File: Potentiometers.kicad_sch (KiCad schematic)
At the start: 20 parts, among them J10 AccelConn, J11 BrakeConn, J12 AccelConn2, J13 BrakeConn2

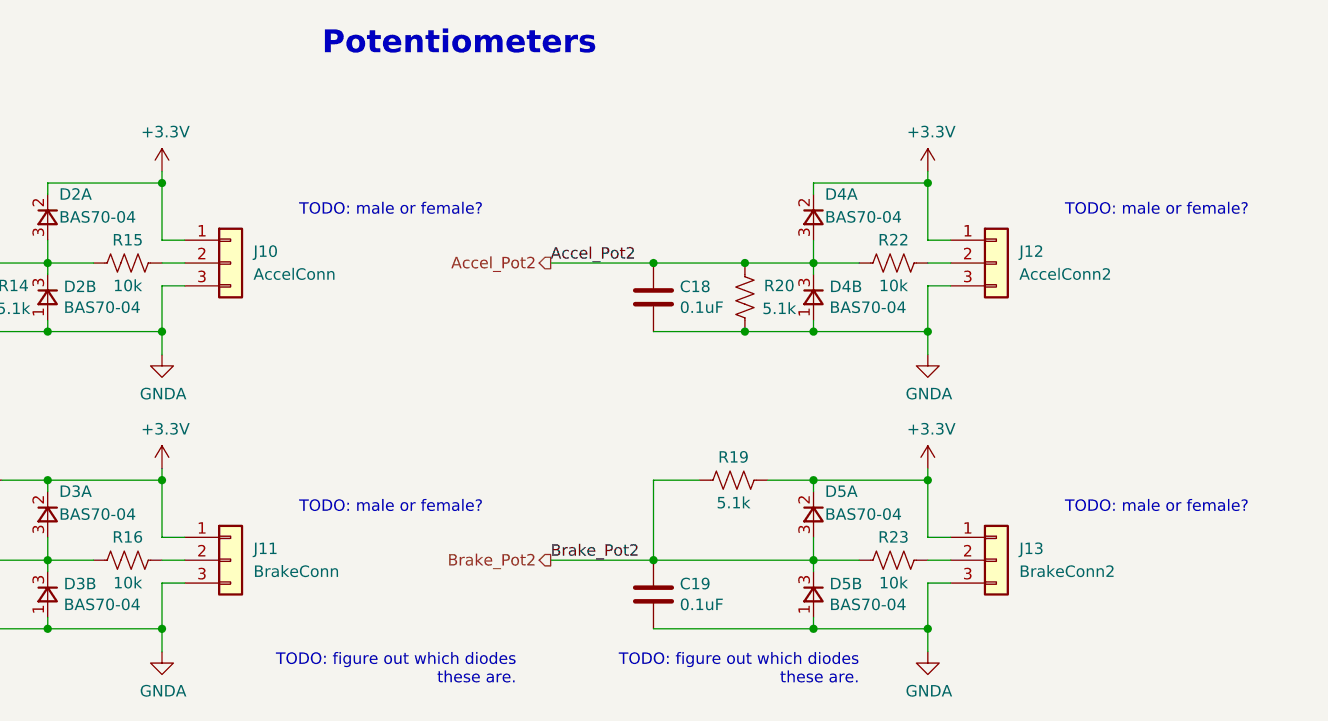
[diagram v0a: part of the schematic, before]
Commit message: Remove 12V isolator, swap CAN connector pins, etc.
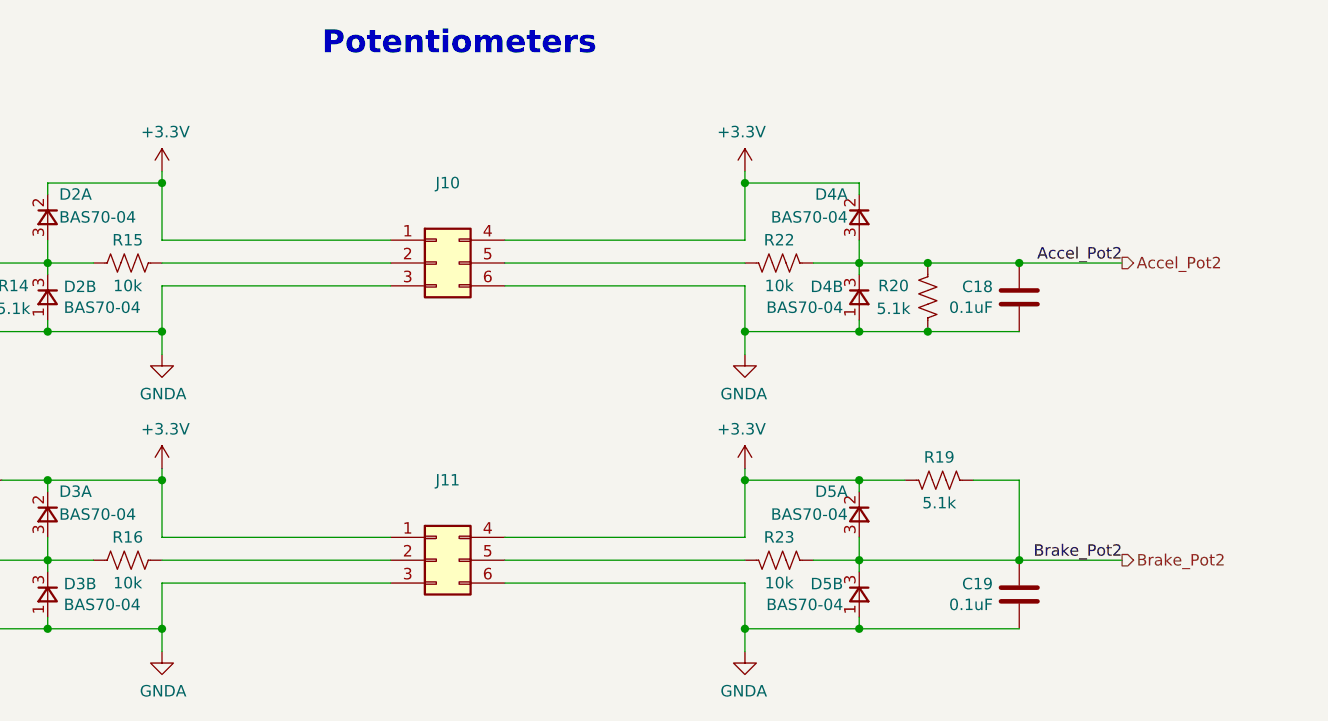
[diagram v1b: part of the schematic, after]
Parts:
- removed J10: AccelConn, UTSVT_Connectors:Molex_MicroFit3.0_1x3xP3.00mm_PolarizingPeg_Vertical, symbol Connector_Generic:Conn_01x03
- removed J11: BrakeConn, UTSVT_Connectors:Molex_MicroFit3.0_1x3xP3.00mm_PolarizingPeg_Vertical, symbol Connector_Generic:Conn_01x03
- removed J12: AccelConn2, UTSVT_Connectors:Molex_MicroFit3.0_1x3xP3.00mm_PolarizingPeg_Vertical, symbol Connector_Generic:Conn_01x03
- removed J13: BrakeConn2, UTSVT_Connectors:Molex_MicroFit3.0_1x3xP3.00mm_PolarizingPeg_Vertical, symbol Connector_Generic:Conn_01x03
- added J10, J11: (no value), symbol Connector_Generic:Conn_02x03_Top_Bottom
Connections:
- net +3V3: now also J10.1 (Pin_1), J10.4 (Pin_4), J11.1 (Pin_1), J11.4 (Pin_4)
- net GNDA: now also J10.3 (Pin_3), J10.6 (Pin_6), J11.3 (Pin_3), J11.6 (Pin_6)
- net at R22.1: now also J10.5 (Pin_5)
- net at R23.1: now also J11.5 (Pin_5)
- net at R15.1: now also J10.2 (Pin_2)
- net at R16.1: now also J11.2 (Pin_2)
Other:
- note removed: "TODO: figure out which diodes these are."
- note removed: "TODO: male or female?"
- moved on the sheet: C18, C19, D4A, D4B, D5A, D5B, R19, R20, R22, R23

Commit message: Release v2.4 and gerbers
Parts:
- J10, J11: value (none) -> Conn_02x03_Top_Bottom; footprint (none) -> Connector_Molex:Molex_Micro-Fit_3.0_43045-0612_2x03_P3.00mm_Vertical
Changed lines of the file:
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@@
     (in_bom yes) (on_board yes) (fields_autoplaced)
     (property "Reference" "J10" (id 0) (at 146.05 71.12 0))
-    (property "Value" "" (id 1) (at 146.05 73.66 0))
-    (property "Footprint" "" (id 2) (at 144.78 80.01 0)
+    (property "Value" "Conn_02x03_Top_Bottom" (id 1) (at 146.05 73.66 0))
+    (property "Footprint" "Connector_Molex:Molex_Micro-Fit_3.0_43045-0612_2x03_P3.00mm_Vertical" (id 2) (at 144.78 80.01 0)
       (effects (font (size 1.27 1.27)) hide)
     )
@@
     (in_bom yes) (on_board yes) (fields_autoplaced)
     (property "Reference" "J11" (id 0) (at 146.05 104.14 0))
-    (property "Value" "" (id 1) (at 146.05 106.68 0))
-    (property "Footprint" "" (id 2) (at 144.78 113.03 0)
+    (property "Value" "Conn_02x03_Top_Bottom" (id 1) (at 146.05 106.68 0))
+    (property "Footprint" "Connector_Molex:Molex_Micro-Fit_3.0_43045-0612_2x03_P3.00mm_Vertical" (id 2) (at 144.78 113.03 0)
       (effects (font (size 1.27 1.27)) hide)
     )

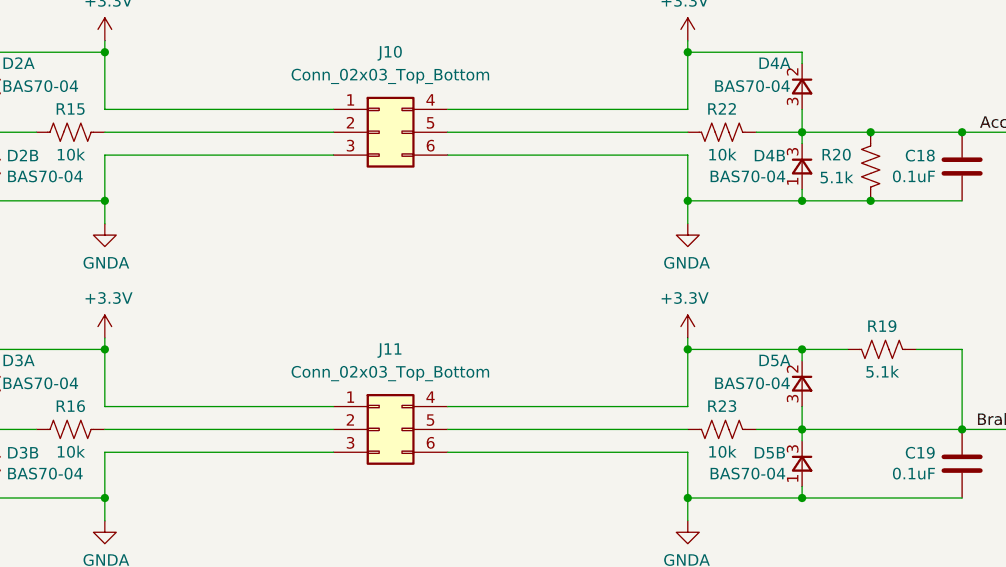
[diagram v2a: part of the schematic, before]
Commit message: Schematic notations for rework changes
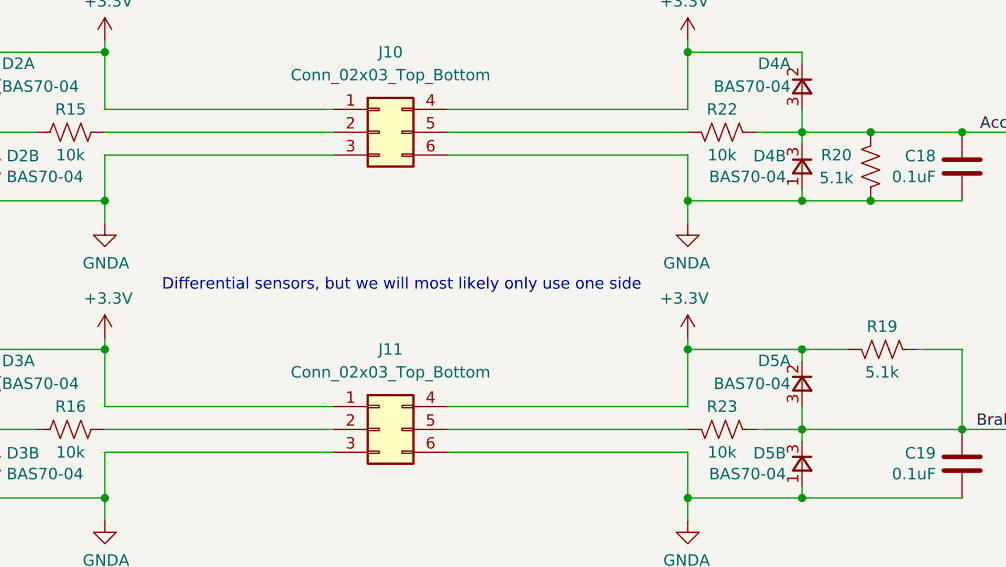
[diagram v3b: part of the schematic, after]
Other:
- note added: "Differential sensors, but we will most likely only use one side"

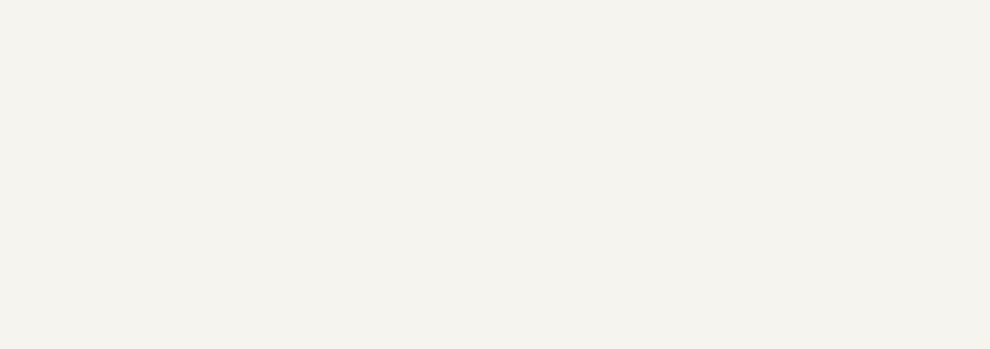
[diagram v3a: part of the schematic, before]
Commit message: Updated schematic in accordance to previous weeks annotated changes
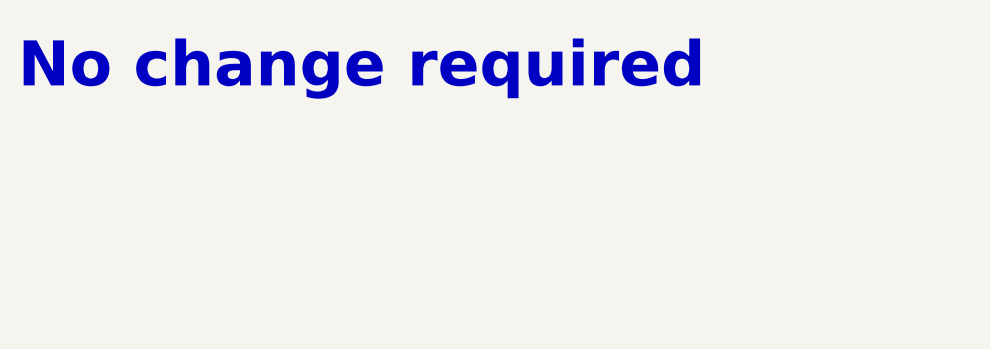
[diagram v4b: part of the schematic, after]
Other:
- note added: "No change required"
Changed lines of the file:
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@@
     (effects (font (size 2.54 2.54) (thickness 0.508) bold) (justify left bottom))
+  )
+  (text "No change required\n" (at 13.97 22.86 0)
+    (effects (font (face "KiCad Font") (size 5 5) (thickness 1) bold (color 255 2 13 1)) (justify left bottom))
   )
   (text "Differential sensors, but we will most likely only use one side\n"

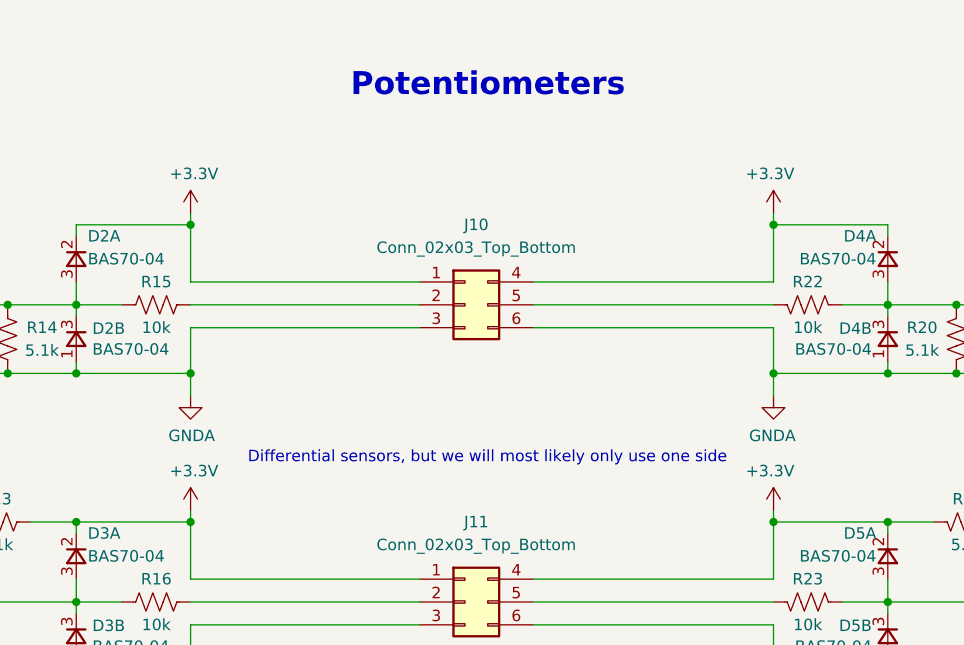
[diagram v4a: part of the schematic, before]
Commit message: Renamed Clk to PA5, removed CAN_TX/RX test points, deleted other .lck file and #auto_saved_files# (hopefully this does not break anything.
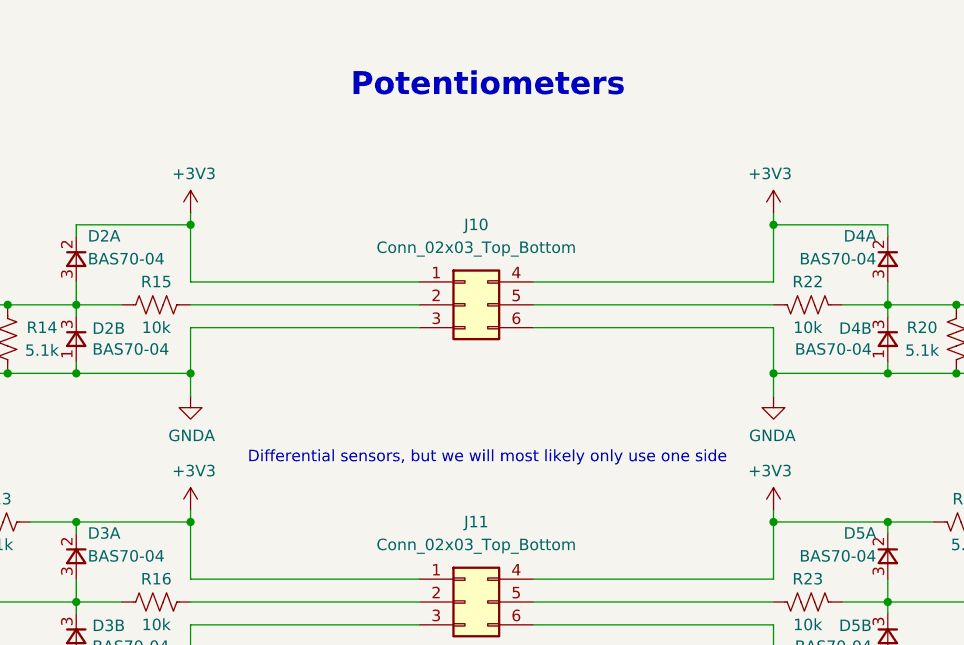
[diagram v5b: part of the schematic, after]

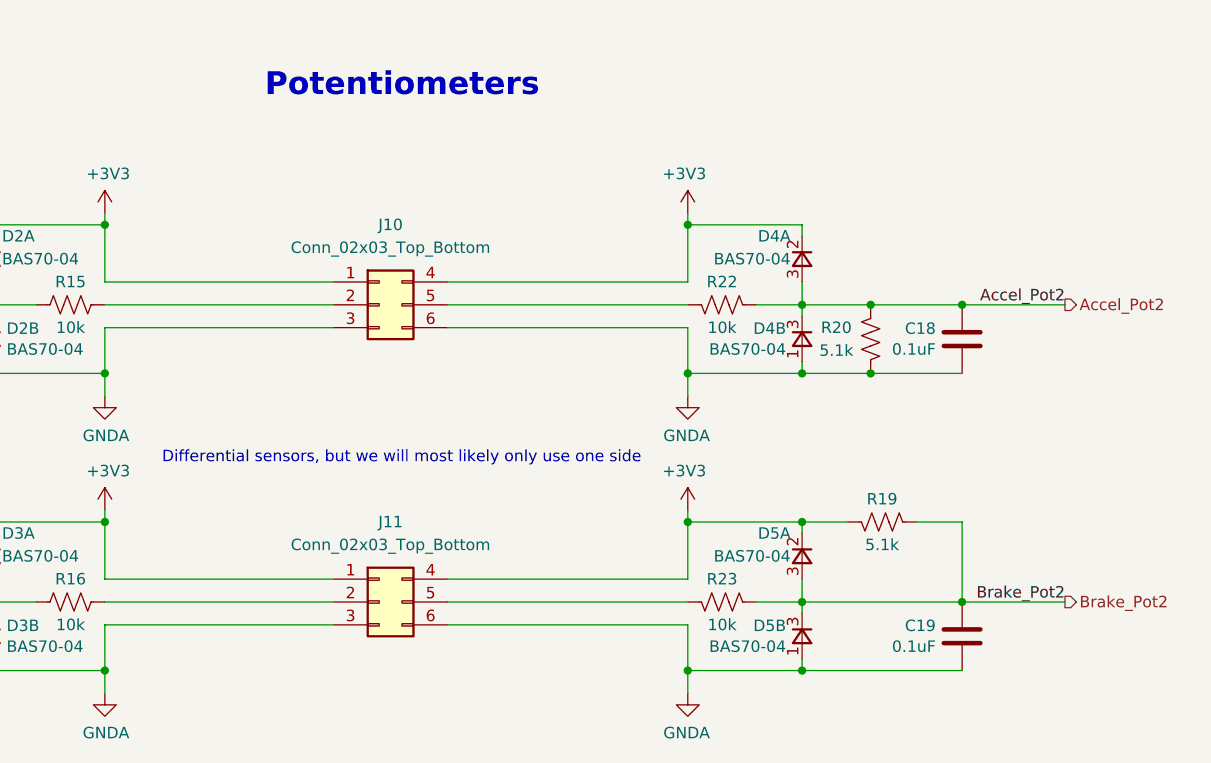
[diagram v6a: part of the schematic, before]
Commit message: renamed power state indicators to contactors and removed unused contactors, added current limiting resistors to lights drivers, changed mosfet to new mosfet
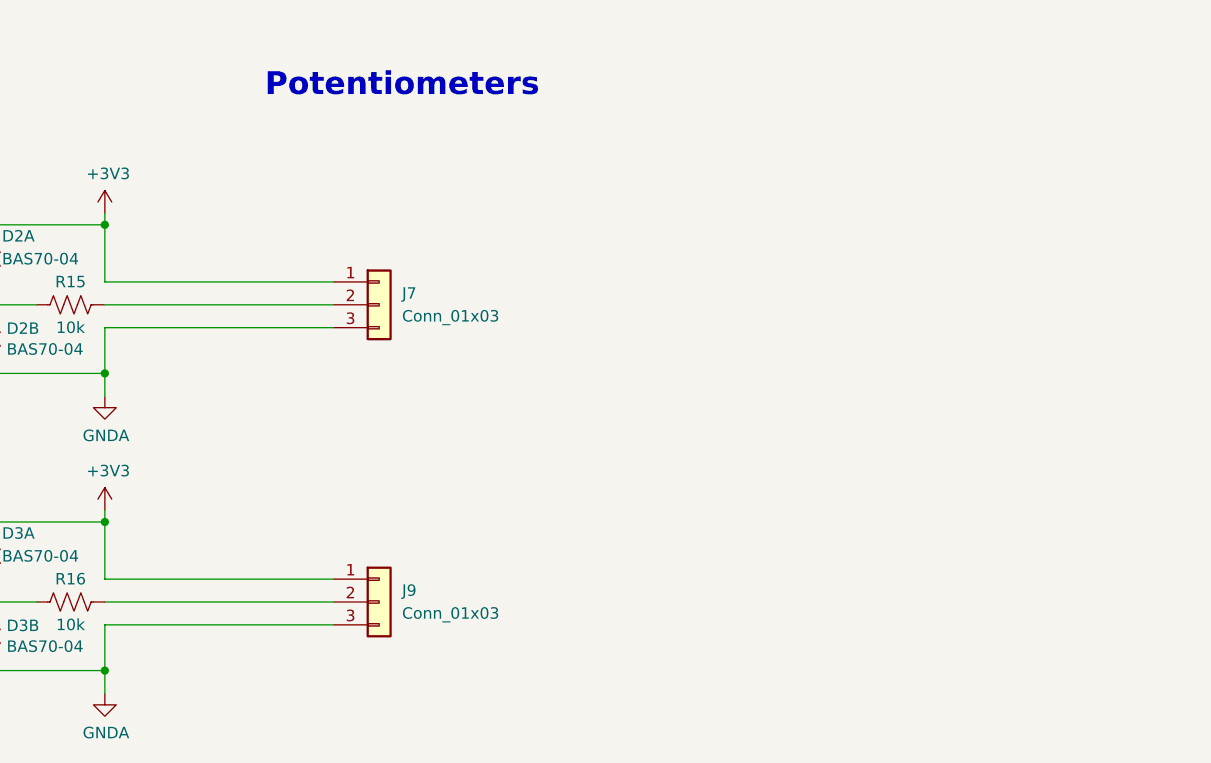
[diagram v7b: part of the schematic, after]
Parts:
- removed C18, C19: 0.1uF, Capacitor_SMD:C_0805_2012Metric, symbol Device:C
- removed D4, D5: BAS70-04, Package_TO_SOT_SMD:SOT-23, symbol Dashboard-rescue:BAS70-04-utsvt-chips
- removed J10, J11: Conn_02x03_Top_Bottom, Connector_Molex:Molex_Micro-Fit_3.0_43045-0612_2x03_P3.00mm_Vertical, symbol Connector_Generic:Conn_02x03_Top_Bottom
- removed R19, R20: 5.1k, Resistor_SMD:R_0805_2012Metric, symbol Device:R_US
- removed R22, R23: 10k, Resistor_SMD:R_0805_2012Metric, symbol Device:R_US
- added J7, J9: Conn_01x03, Connector_Molex:Molex_Micro-Fit_3.0_43650-0315_1x03_P3.00mm_Vertical, symbol Connector_Generic:Conn_01x03
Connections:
- net +3V3: now also J7.1 (Pin_1), J9.1 (Pin_1)
- net GNDA: now also J7.3 (Pin_3), J9.3 (Pin_3)
- net at R16.1: now also J9.2 (Pin_2)
- net at R15.1: now also J7.2 (Pin_2)
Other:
- note removed: "Differential sensors, but we will most likely only use one side"
